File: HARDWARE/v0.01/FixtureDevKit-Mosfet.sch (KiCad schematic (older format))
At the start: 40 parts

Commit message: o boy
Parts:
- TP?: value TEST -> G0
- TP?: value TEST -> G1
- TP?: value TEST -> G2
- TP? (x2): value TEST -> G3
- TP?: value TEST -> G4
- TP?: value TEST -> G5
- TP?: value TEST -> G6
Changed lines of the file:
@@
 P 2400 2550
 F 0 "TP?" H 2400 2850 50  0000 C BNN
-F 1 "TEST" H 2400 2800 50  0000 C CNN
+F 1 "G0" H 2400 2800 50  0000 C CNN
 F 2 "" H 2400 2550 50  0001 C CNN
 F 3 "" H 2400 2550 50  0001 C CNN
@@
 P 4300 2550
 F 0 "TP?" H 4300 2850 50  0000 C BNN
-F 1 "TEST" H 4300 2800 50  0000 C CNN
+F 1 "G1" H 4300 2800 50  0000 C CNN
 F 2 "" H 4300 2550 50  0001 C CNN
 F 3 "" H 4300 2550 50  0001 C CNN
@@
 P 6850 2550
 F 0 "TP?" H 6850 2850 50  0000 C BNN
-F 1 "TEST" H 6850 2800 50  0000 C CNN
+F 1 "G2" H 6850 2800 50  0000 C CNN
 F 2 "" H 6850 2550 50  0001 C CNN
 F 3 "" H 6850 2550 50  0001 C CNN
@@
 P 8750 2550
 F 0 "TP?" H 8750 2850 50  0000 C BNN
-F 1 "TEST" H 8750 2800 50  0000 C CNN
+F 1 "G3" H 8750 2800 50  0000 C CNN
 F 2 "" H 8750 2550 50  0001 C CNN
 F 3 "" H 8750 2550 50  0001 C CNN
@@
 P 2400 5000
 F 0 "TP?" H 2400 5300 50  0000 C BNN
-F 1 "TEST" H 2400 5250 50  0000 C CNN
+F 1 "G3" H 2400 5250 50  0000 C CNN
 F 2 "" H 2400 5000 50  0001 C CNN
 F 3 "" H 2400 5000 50  0001 C CNN
@@
 P 4300 5000
 F 0 "TP?" H 4300 5300 50  0000 C BNN
-F 1 "TEST" H 4300 5250 50  0000 C CNN
+F 1 "G4" H 4300 5250 50  0000 C CNN
 F 2 "" H 4300 5000 50  0001 C CNN
 F 3 "" H 4300 5000 50  0001 C CNN
@@
 P 6850 5000
 F 0 "TP?" H 6850 5300 50  0000 C BNN
-F 1 "TEST" H 6850 5250 50  0000 C CNN
+F 1 "G5" H 6850 5250 50  0000 C CNN
 F 2 "" H 6850 5000 50  0001 C CNN
 F 3 "" H 6850 5000 50  0001 C CNN
@@
 P 8750 5000
 F 0 "TP?" H 8750 5300 50  0000 C BNN
-F 1 "TEST" H 8750 5250 50  0000 C CNN
+F 1 "G6" H 8750 5250 50  0000 C CNN
 F 2 "" H 8750 5000 50  0001 C CNN
 F 3 "" H 8750 5000 50  0001 C CNN

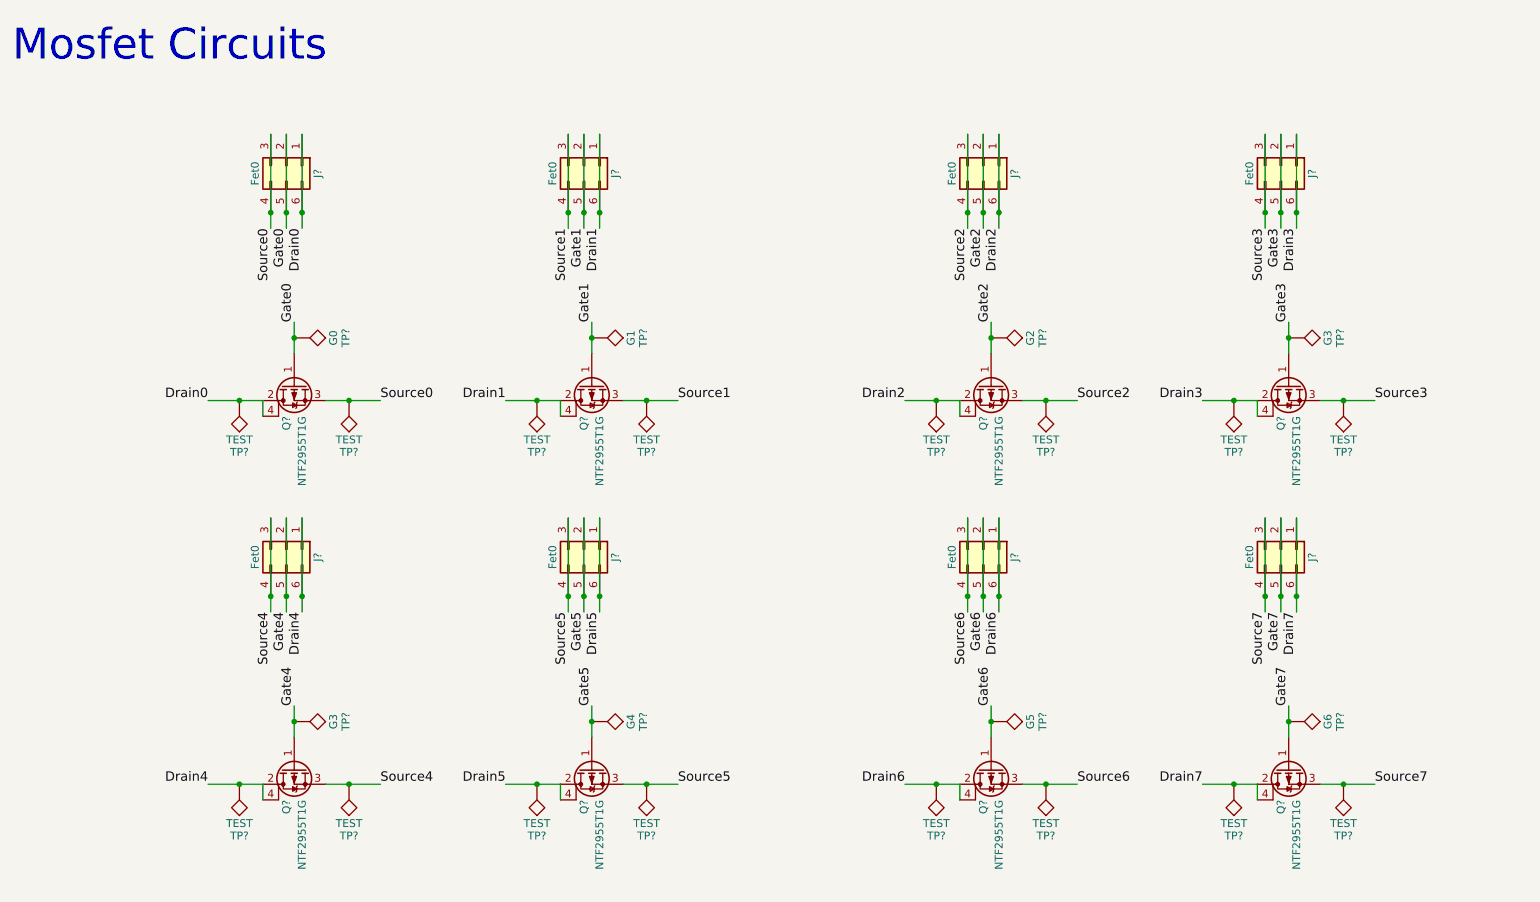
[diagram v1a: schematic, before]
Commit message: adding netlist and design rules check
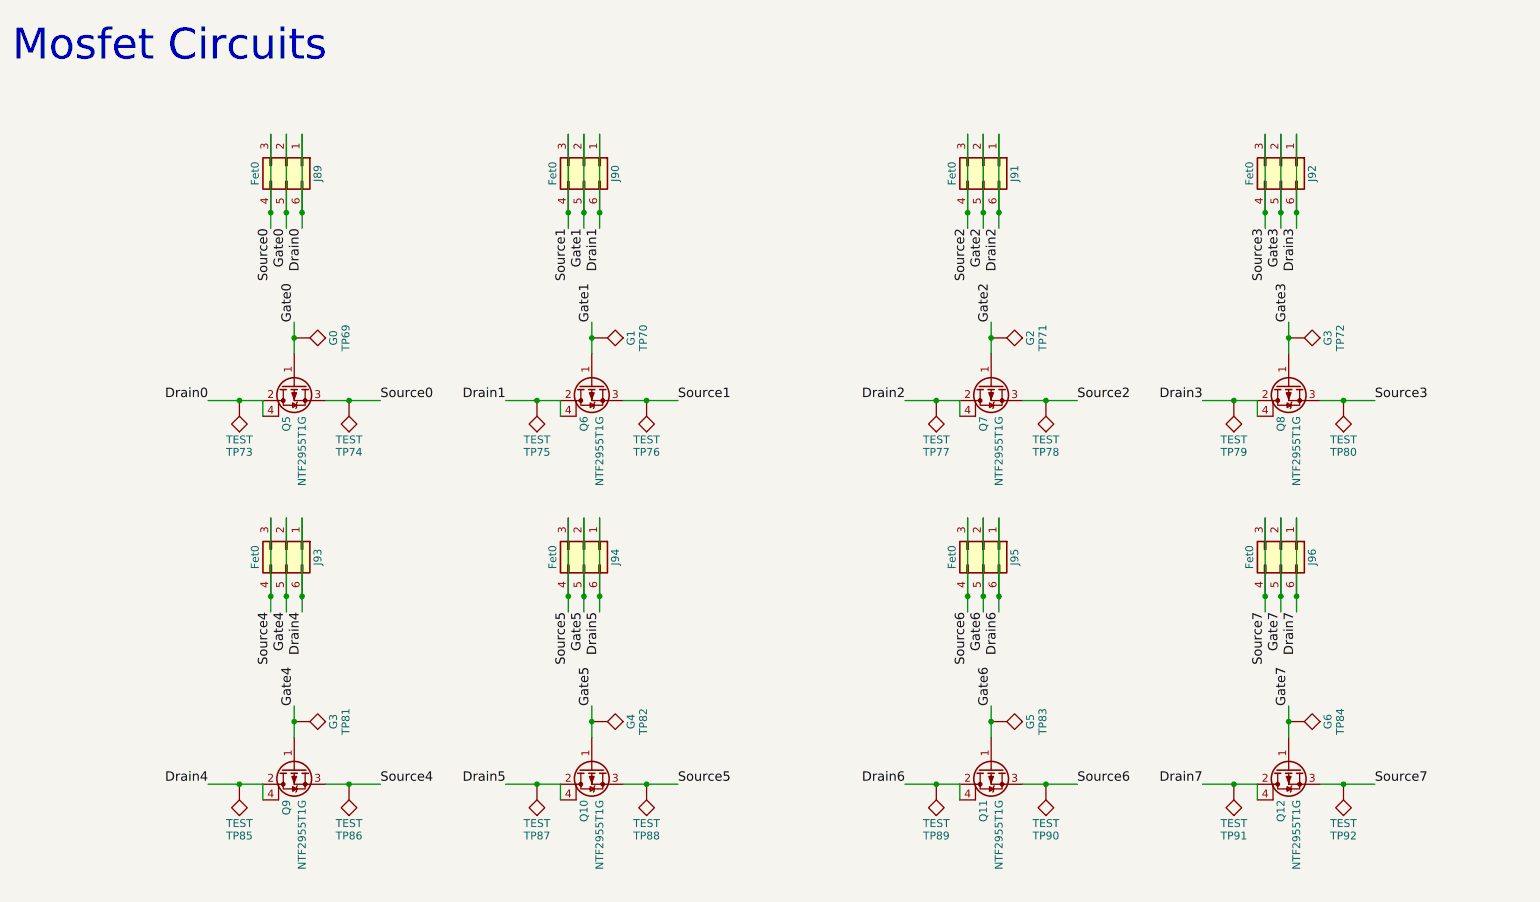
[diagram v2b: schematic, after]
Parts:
- gave numbers to parts that had none: 40
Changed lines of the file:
@@
 $EndDescr
 $Comp
-L Q_PMOS_GDSD Q?
+L Q_PMOS_GDSD Q5
 U 1 1 59F00EBB
 P 2400 2850
-F 0 "Q?" H 2600 2900 50  0000 L CNN
+F 0 "Q5" H 2600 2900 50  0000 L CNN
 F 1 "NTF2955T1G" H 2600 2800 50  0000 L CNN
 F 2 "" H 2600 2950 50  0001 C CNN
@@
 $EndComp
 $Comp
-L TEST TP?
+L TEST TP69
 U 1 1 59F010EC
 P 2400 2550
-F 0 "TP?" H 2400 2850 50  0000 C BNN
+F 0 "TP69" H 2400 2850 50  0000 C BNN
 F 1 "G0" H 2400 2800 50  0000 C CNN
 F 2 "" H 2400 2550 50  0001 C CNN
@@
 $EndComp
 $Comp
-L TEST TP?
+L TEST TP74
 U 1 1 59F01148
 P 2750 2950
-F 0 "TP?" H 2750 3250 50  0000 C BNN
+F 0 "TP74" H 2750 3250 50  0000 C BNN
 F 1 "TEST" H 2750 3200 50  0000 C CNN
 F 2 "" H 2750 2950 50  0001 C CNN
@@
 $EndComp
 $Comp
-L TEST TP?
+L TEST TP73
 U 1 1 59F01182
 P 2050 2950
-F 0 "TP?" H 2050 3250 50  0000 C BNN
+F 0 "TP73" H 2050 3250 50  0000 C BNN
 F 1 "TEST" H 2050 3200 50  0000 C CNN
 F 2 "" H 2050 2950 50  0001 C CNN
@@
 Drain0
 $Comp
-L Conn_02x03_Counter_Clockwise J?
+L Conn_02x03_Counter_Clockwise J89
 U 1 1 59F012B7
 P 2350 1450
-F 0 "J?" H 2400 1650 50  0000 C CNN
+F 0 "J89" H 2400 1650 50  0000 C CNN
 F 1 "Fet0" H 2400 1250 50  0000 C CNN
 F 2 "" H 2350 1450 50  0001 C CNN
@@
 Connection ~ 2250 1750
 $Comp
-L Q_PMOS_GDSD Q?
+L Q_PMOS_GDSD Q6
 U 1 1 59F01C9D
 P 4300 2850
-F 0 "Q?" H 4500 2900 50  0000 L CNN
+F 0 "Q6" H 4500 2900 50  0000 L CNN
 F 1 "NTF2955T1G" H 4500 2800 50  0000 L CNN
 F 2 "" H 4500 2950 50  0001 C CNN
@@
 $EndComp
 $Comp
-L TEST TP?
+L TEST TP70
 U 1 1 59F01CA3
 P 4300 2550
-F 0 "TP?" H 4300 2850 50  0000 C BNN
+F 0 "TP70" H 4300 2850 50  0000 C BNN
 F 1 "G1" H 4300 2800 50  0000 C CNN
 F 2 "" H 4300 2550 50  0001 C CNN
@@
 $EndComp
 $Comp
-L TEST TP?
+L TEST TP76
 U 1 1 59F01CA9
 P 4650 2950
-F 0 "TP?" H 4650 3250 50  0000 C BNN
+F 0 "TP76" H 4650 3250 50  0000 C BNN
 F 1 "TEST" H 4650 3200 50  0000 C CNN
 F 2 "" H 4650 2950 50  0001 C CNN
@@
 $EndComp
 $Comp
-L TEST TP?
+L TEST TP75
 U 1 1 59F01CAF
 P 3950 2950
-F 0 "TP?" H 3950 3250 50  0000 C BNN
+F 0 "TP75" H 3950 3250 50  0000 C BNN
 F 1 "TEST" H 3950 3200 50  0000 C CNN
 F 2 "" H 3950 2950 50  0001 C CNN
@@
 Drain1
 $Comp
-L Conn_02x03_Counter_Clockwise J?
+L Conn_02x03_Counter_Clockwise J90
 U 1 1 59F01CB7
 P 4250 1450
-F 0 "J?" H 4300 1650 50  0000 C CNN
+F 0 "J90" H 4300 1650 50  0000 C CNN
 F 1 "Fet0" H 4300 1250 50  0000 C CNN
 F 2 "" H 4250 1450 50  0001 C CNN
@@
 Connection ~ 4150 1750
 $Comp
-L Q_PMOS_GDSD Q?
+L Q_PMOS_GDSD Q7
 U 1 1 59F02962
 P 6850 2850
-F 0 "Q?" H 7050 2900 50  0000 L CNN
+F 0 "Q7" H 7050 2900 50  0000 L CNN
 F 1 "NTF2955T1G" H 7050 2800 50  0000 L CNN
 F 2 "" H 7050 2950 50  0001 C CNN
@@
 $EndComp
 $Comp
-L TEST TP?
+L TEST TP71
 U 1 1 59F02968
 P 6850 2550
-F 0 "TP?" H 6850 2850 50  0000 C BNN
+F 0 "TP71" H 6850 2850 50  0000 C BNN
 F 1 "G2" H 6850 2800 50  0000 C CNN
 F 2 "" H 6850 2550 50  0001 C CNN
@@
 $EndComp
 $Comp
-L TEST TP?
+L TEST TP78
 U 1 1 59F0296E
 P 7200 2950
-F 0 "TP?" H 7200 3250 50  0000 C BNN
+F 0 "TP78" H 7200 3250 50  0000 C BNN
 F 1 "TEST" H 7200 3200 50  0000 C CNN
 F 2 "" H 7200 2950 50  0001 C CNN
@@
 $EndComp
 $Comp
-L TEST TP?
+L TEST TP77
 U 1 1 59F02974
 P 6500 2950
-F 0 "TP?" H 6500 3250 50  0000 C BNN
+F 0 "TP77" H 6500 3250 50  0000 C BNN
 F 1 "TEST" H 6500 3200 50  0000 C CNN
 F 2 "" H 6500 2950 50  0001 C CNN
@@
 Drain2
 $Comp
-L Conn_02x03_Counter_Clockwise J?
+L Conn_02x03_Counter_Clockwise J91
 U 1 1 59F0297C
 P 6800 1450
-F 0 "J?" H 6850 1650 50  0000 C CNN
+F 0 "J91" H 6850 1650 50  0000 C CNN
 F 1 "Fet0" H 6850 1250 50  0000 C CNN
 F 2 "" H 6800 1450 50  0001 C CNN
@@
 Connection ~ 6700 1750
 $Comp
-L Q_PMOS_GDSD Q?
+L Q_PMOS_GDSD Q8
 U 1 1 59F02993
 P 8750 2850
-F 0 "Q?" H 8950 2900 50  0000 L CNN
+F 0 "Q8" H 8950 2900 50  0000 L CNN
 F 1 "NTF2955T1G" H 8950 2800 50  0000 L CNN
 F 2 "" H 8950 2950 50  0001 C CNN
@@
 $EndComp
 $Comp
-L TEST TP?
+L TEST TP72
 U 1 1 59F02999
 P 8750 2550
-F 0 "TP?" H 8750 2850 50  0000 C BNN
+F 0 "TP72" H 8750 2850 50  0000 C BNN
 F 1 "G3" H 8750 2800 50  0000 C CNN
 F 2 "" H 8750 2550 50  0001 C CNN
@@
 $EndComp
 $Comp
-L TEST TP?
+L TEST TP80
 U 1 1 59F0299F
 P 9100 2950
-F 0 "TP?" H 9100 3250 50  0000 C BNN
+F 0 "TP80" H 9100 3250 50  0000 C BNN
 F 1 "TEST" H 9100 3200 50  0000 C CNN
 F 2 "" H 9100 2950 50  0001 C CNN
@@
 $EndComp
 $Comp
-L TEST TP?
+L TEST TP79
 U 1 1 59F029A5
 P 8400 2950
-F 0 "TP?" H 8400 3250 50  0000 C BNN
+F 0 "TP79" H 8400 3250 50  0000 C BNN
 F 1 "TEST" H 8400 3200 50  0000 C CNN
 F 2 "" H 8400 2950 50  0001 C CNN
@@
 Drain3
 $Comp
-L Conn_02x03_Counter_Clockwise J?
+L Conn_02x03_Counter_Clockwise J92
 U 1 1 59F029AD
 P 8700 1450
-F 0 "J?" H 8750 1650 50  0000 C CNN
+F 0 "J92" H 8750 1650 50  0000 C CNN
 F 1 "Fet0" H 8750 1250 50  0000 C CNN
 F 2 "" H 8700 1450 50  0001 C CNN
@@
 Connection ~ 8600 1750
 $Comp
-L Q_PMOS_GDSD Q?
+L Q_PMOS_GDSD Q9
 U 1 1 59F02E9C
 P 2400 5300
-F 0 "Q?" H 2600 5350 50  0000 L CNN
+F 0 "Q9" H 2600 5350 50  0000 L CNN
 F 1 "NTF2955T1G" H 2600 5250 50  0000 L CNN
 F 2 "" H 2600 5400 50  0001 C CNN
@@
 $EndComp
 $Comp
-L TEST TP?
+L TEST TP81
 U 1 1 59F02EA2
 P 2400 5000
-F 0 "TP?" H 2400 5300 50  0000 C BNN
+F 0 "TP81" H 2400 5300 50  0000 C BNN
 F 1 "G3" H 2400 5250 50  0000 C CNN
 F 2 "" H 2400 5000 50  0001 C CNN
@@
 $EndComp
 $Comp
-L TEST TP?
+L TEST TP86
 U 1 1 59F02EA8
 P 2750 5400
-F 0 "TP?" H 2750 5700 50  0000 C BNN
+F 0 "TP86" H 2750 5700 50  0000 C BNN
 F 1 "TEST" H 2750 5650 50  0000 C CNN
 F 2 "" H 2750 5400 50  0001 C CNN
@@
 $EndComp
 $Comp
-L TEST TP?
+L TEST TP85
 U 1 1 59F02EAE
 P 2050 5400
-F 0 "TP?" H 2050 5700 50  0000 C BNN
+F 0 "TP85" H 2050 5700 50  0000 C BNN
 F 1 "TEST" H 2050 5650 50  0000 C CNN
 F 2 "" H 2050 5400 50  0001 C CNN
@@
 Drain4
 $Comp
-L Conn_02x03_Counter_Clockwise J?
+L Conn_02x03_Counter_Clockwise J93
 U 1 1 59F02EB6
 P 2350 3900
-F 0 "J?" H 2400 4100 50  0000 C CNN
+F 0 "J93" H 2400 4100 50  0000 C CNN
 F 1 "Fet0" H 2400 3700 50  0000 C CNN
 F 2 "" H 2350 3900 50  0001 C CNN
@@
 Connection ~ 2250 4200
 $Comp
-L Q_PMOS_GDSD Q?
+L Q_PMOS_GDSD Q10
 U 1 1 59F02ECD
 P 4300 5300
-F 0 "Q?" H 4500 5350 50  0000 L CNN
+F 0 "Q10" H 4500 5350 50  0000 L CNN
 F 1 "NTF2955T1G" H 4500 5250 50  0000 L CNN
 F 2 "" H 4500 5400 50  0001 C CNN
@@
 $EndComp
 $Comp
-L TEST TP?
+L TEST TP82
 U 1 1 59F02ED3
 P 4300 5000
-F 0 "TP?" H 4300 5300 50  0000 C BNN
+F 0 "TP82" H 4300 5300 50  0000 C BNN
 F 1 "G4" H 4300 5250 50  0000 C CNN
 F 2 "" H 4300 5000 50  0001 C CNN
@@
 $EndComp
 $Comp
-L TEST TP?
+L TEST TP88
 U 1 1 59F02ED9
 P 4650 5400
-F 0 "TP?" H 4650 5700 50  0000 C BNN
+F 0 "TP88" H 4650 5700 50  0000 C BNN
 F 1 "TEST" H 4650 5650 50  0000 C CNN
 F 2 "" H 4650 5400 50  0001 C CNN
@@
 $EndComp
 $Comp
-L TEST TP?
+L TEST TP87
 U 1 1 59F02EDF
 P 3950 5400
-F 0 "TP?" H 3950 5700 50  0000 C BNN
+F 0 "TP87" H 3950 5700 50  0000 C BNN
 F 1 "TEST" H 3950 5650 50  0000 C CNN
 F 2 "" H 3950 5400 50  0001 C CNN
@@
 Drain5
 $Comp
-L Conn_02x03_Counter_Clockwise J?
+L Conn_02x03_Counter_Clockwise J94
 U 1 1 59F02EE7
 P 4250 3900
-F 0 "J?" H 4300 4100 50  0000 C CNN
+F 0 "J94" H 4300 4100 50  0000 C CNN
 F 1 "Fet0" H 4300 3700 50  0000 C CNN
 F 2 "" H 4250 3900 50  0001 C CNN
@@
 Connection ~ 4150 4200
 $Comp
-L Q_PMOS_GDSD Q?
+L Q_PMOS_GDSD Q11
 U 1 1 59F02EFE
 P 6850 5300
-F 0 "Q?" H 7050 5350 50  0000 L CNN
+F 0 "Q11" H 7050 5350 50  0000 L CNN
 F 1 "NTF2955T1G" H 7050 5250 50  0000 L CNN
 F 2 "" H 7050 5400 50  0001 C CNN
@@
 $EndComp
 $Comp
-L TEST TP?
+L TEST TP83
 U 1 1 59F02F04
 P 6850 5000
-F 0 "TP?" H 6850 5300 50  0000 C BNN
+F 0 "TP83" H 6850 5300 50  0000 C BNN
 F 1 "G5" H 6850 5250 50  0000 C CNN
 F 2 "" H 6850 5000 50  0001 C CNN
@@
 $EndComp
 $Comp
-L TEST TP?
+L TEST TP90
 U 1 1 59F02F0A
 P 7200 5400
-F 0 "TP?" H 7200 5700 50  0000 C BNN
+F 0 "TP90" H 7200 5700 50  0000 C BNN
 F 1 "TEST" H 7200 5650 50  0000 C CNN
 F 2 "" H 7200 5400 50  0001 C CNN
@@
 $EndComp
 $Comp
-L TEST TP?
+L TEST TP89
 U 1 1 59F02F10
 P 6500 5400
-F 0 "TP?" H 6500 5700 50  0000 C BNN
+F 0 "TP89" H 6500 5700 50  0000 C BNN
 F 1 "TEST" H 6500 5650 50  0000 C CNN
 F 2 "" H 6500 5400 50  0001 C CNN
@@
 Drain6
 $Comp
-L Conn_02x03_Counter_Clockwise J?
+L Conn_02x03_Counter_Clockwise J95
 U 1 1 59F02F18
 P 6800 3900
-F 0 "J?" H 6850 4100 50  0000 C CNN
+F 0 "J95" H 6850 4100 50  0000 C CNN
 F 1 "Fet0" H 6850 3700 50  0000 C CNN
 F 2 "" H 6800 3900 50  0001 C CNN
@@
 Connection ~ 6700 4200
 $Comp
-L Q_PMOS_GDSD Q?
+L Q_PMOS_GDSD Q12
 U 1 1 59F02F2F
 P 8750 5300
-F 0 "Q?" H 8950 5350 50  0000 L CNN
+F 0 "Q12" H 8950 5350 50  0000 L CNN
 F 1 "NTF2955T1G" H 8950 5250 50  0000 L CNN
 F 2 "" H 8950 5400 50  0001 C CNN
@@
 $EndComp
 $Comp
-L TEST TP?
+L TEST TP84
 U 1 1 59F02F35
 P 8750 5000
-F 0 "TP?" H 8750 5300 50  0000 C BNN
+F 0 "TP84" H 8750 5300 50  0000 C BNN
 F 1 "G6" H 8750 5250 50  0000 C CNN
 F 2 "" H 8750 5000 50  0001 C CNN
@@
 $EndComp
 $Comp
-L TEST TP?
+L TEST TP92
 U 1 1 59F02F3B
 P 9100 5400
-F 0 "TP?" H 9100 5700 50  0000 C BNN
+F 0 "TP92" H 9100 5700 50  0000 C BNN
 F 1 "TEST" H 9100 5650 50  0000 C CNN
 F 2 "" H 9100 5400 50  0001 C CNN
@@
 $EndComp
 $Comp
-L TEST TP?
+L TEST TP91
 U 1 1 59F02F41
 P 8400 5400
-F 0 "TP?" H 8400 5700 50  0000 C BNN
+F 0 "TP91" H 8400 5700 50  0000 C BNN
 F 1 "TEST" H 8400 5650 50  0000 C CNN
 F 2 "" H 8400 5400 50  0001 C CNN
@@
 Drain7
 $Comp
-L Conn_02x03_Counter_Clockwise J?
+L Conn_02x03_Counter_Clockwise J96
 U 1 1 59F02F49
 P 8700 3900
-F 0 "J?" H 8750 4100 50  0000 C CNN
+F 0 "J96" H 8750 4100 50  0000 C CNN
 F 1 "Fet0" H 8750 3700 50  0000 C CNN
 F 2 "" H 8700 3900 50  0001 C CNN

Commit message: updating a few blocks, adding test points
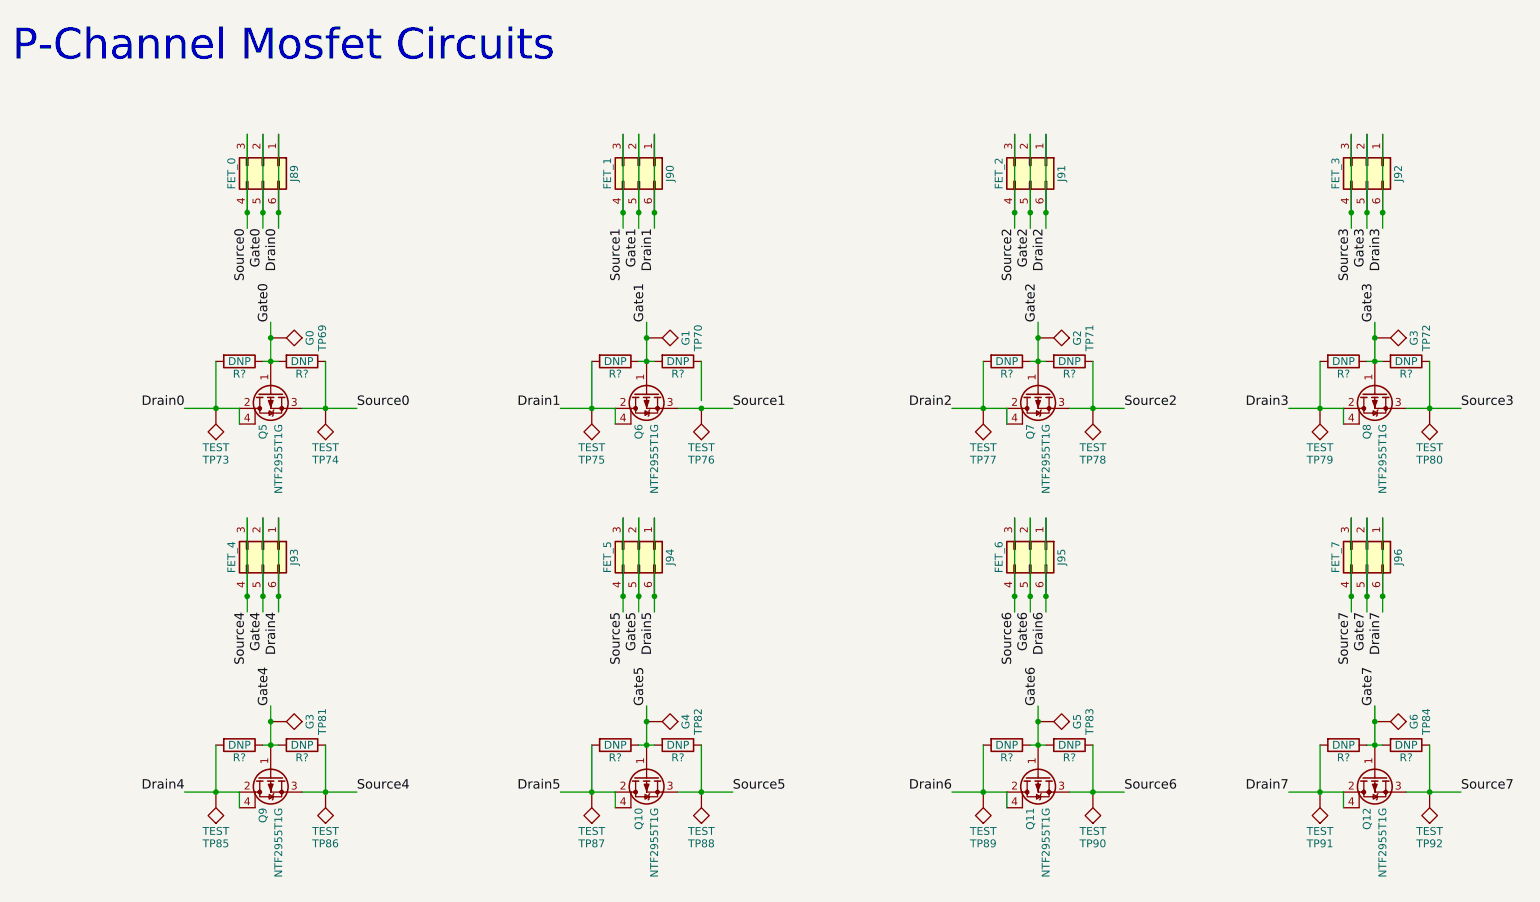
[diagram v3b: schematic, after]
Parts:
- added R? (x16): DNP, symbol R
- J89: value Fet0 -> FET_0
- J90: value Fet0 -> FET_1
- J91: value Fet0 -> FET_2
- J92: value Fet0 -> FET_3
- J93: value Fet0 -> FET_4
- J94: value Fet0 -> FET_5
- J95: value Fet0 -> FET_6
- J96: value Fet0 -> FET_7
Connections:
- net Drain0: now also R?.2
- net Drain1: now also R?.2
- net Drain2: now also R?.2
- net Drain3: now also R?.2
- net Drain4: now also R?.2
- net Drain5: now also R?.2
- net Drain6: now also R?.2
- net Drain7: now also R?.2
- net Gate0: now also R?.1, R?.2
- net Gate1: now also R?.1, R?.2
- net Gate2: now also R?.1, R?.2
- net Gate3: now also R?.1, R?.2
- net Gate4: now also R?.1, R?.2
- net Gate5: now also R?.1, R?.2
- net Gate6: now also R?.1, R?.2
- net Gate7: now also R?.1, R?.2
- net Source0: now also R?.1
- net Source2: now also R?.1
- net Source3: now also R?.1
- net Source4: now also R?.1
- net Source5: now also R?.1
- net Source6: now also R?.1
- net Source7: now also R?.1
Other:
- note added: "P-Channel Mosfet Circuits\n"
- note removed: "Mosfet Circuits\n"
- moved on the sheet: J89, J90, J91, J92, J93, J94, J95, J96, Q10, Q11, Q12, Q5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
